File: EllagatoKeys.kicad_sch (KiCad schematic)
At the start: 23 parts, among them J1 Conn_01x10_Socket, SW1 SW_SPST, SW2 SW_SPST, SW3 SW_SPST, SW4 SW_SPST, SW5 RotaryEncoder_Switch_MP, U2 74AHCT1G125

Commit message: Production V1
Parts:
- removed J1: Conn_01x10_Socket, Connector_PinHeader_2.54mm:PinHeader_1x10_P2.54mm_Horizontal, symbol Connector:Conn_01x10_Socket
- added C1: 100n, Capacitor_SMD:C_0805_2012Metric_Pad1.18x1.45mm_HandSolder, symbol Device:C_Small
- added J2: Conn_01x08_Socket, Connector_PinHeader_2.54mm:PinHeader_1x08_P2.54mm_Horizontal, symbol Connector:Conn_01x08_Socket
- added R1: 10k, Resistor_SMD:R_0805_2012Metric_Pad1.20x1.40mm_HandSolder, symbol Device:R_Small
- added TP0: Ground, TestPoint:TestPoint_Keystone_5010-5014_Multipurpose, symbol Connector:TestPoint
- added TP1: LED Data In, TestPoint:TestPoint_Keystone_5010-5014_Multipurpose, symbol Connector:TestPoint_Probe
- added TP2: REnc A, TestPoint:TestPoint_Keystone_5010-5014_Multipurpose, symbol Connector:TestPoint_Probe
- added TP3: REnc B, TestPoint:TestPoint_Keystone_5010-5014_Multipurpose, symbol Connector:TestPoint_Probe
- added TP4: SR PL, TestPoint:TestPoint_Keystone_5010-5014_Multipurpose, symbol Connector:TestPoint_Probe
- added TP5: SR CLK, TestPoint:TestPoint_Keystone_5010-5014_Multipurpose, symbol Connector:TestPoint_Probe
- added TP6: SR DATA, TestPoint:TestPoint_Keystone_5010-5014_Multipurpose, symbol Connector:TestPoint_Probe
- added U1: 74HC165, Package_SO:SOIC-16_3.9x9.9mm_P1.27mm, symbol 74xx:74HC165
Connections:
- net +5V: now also C1.2, J2.8 (Pin_8), U1.16 (VCC)
- net Enc_A: now also J2.5 (Pin_5), TP2.1, U1.4 (D5)
- net Enc_B: now also J2.6 (Pin_6), TP3.1, U1.5 (D6)
- net Enc_Btn: now also U1.3 (D4)
- net GND: now also C1.1, J2.1 (Pin_1), R1.1, TP0.1, U1.15 (~{CE}), U1.8 (GND)
- net Led_Input: now also J2.7 (Pin_7)
- net btn_A: now also U1.12 (D1)
- net btn_B: now also U1.13 (D2)
- net btn_C: now also U1.14 (D3)
- net btn_OnOff: now also U1.11 (D0)
- net at LED5.3 (DIN), U2.4: now also TP1.1
- new net: R1.2, U1.6 (D7)
- new net SR_CK: J2.3 (Pin_3), TP5.1, U1.2 (CP)
- new net SR_D: J2.2 (Pin_2), TP6.1, U1.9 (Q7)
- new net SR_PL: J2.4 (Pin_4), TP4.1, U1.1 (~{PL})
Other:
- moved on the sheet: R10, R11, R8, R9, SW1, SW2, SW3, SW4

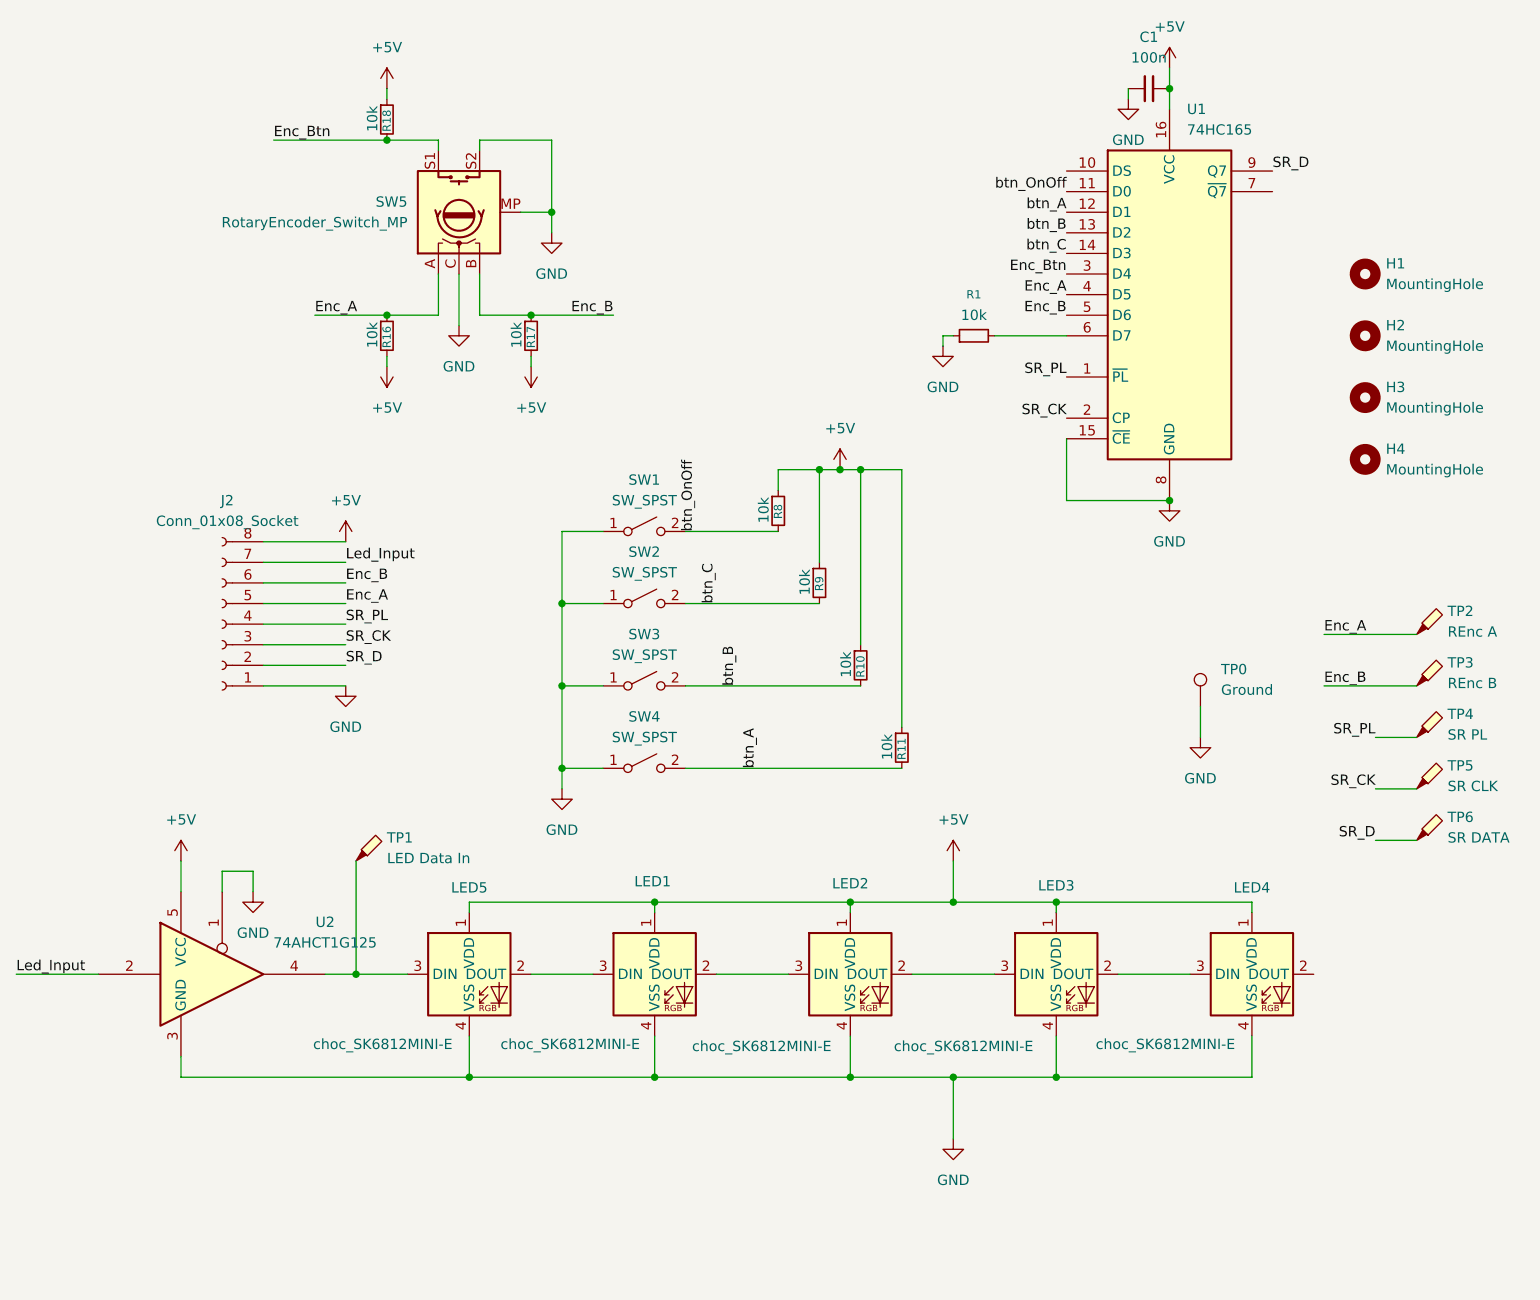
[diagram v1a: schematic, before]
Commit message: +Added Decoupling Cap to LED !!Added connection to VCC for LED2&3 !Restored compoenent labels
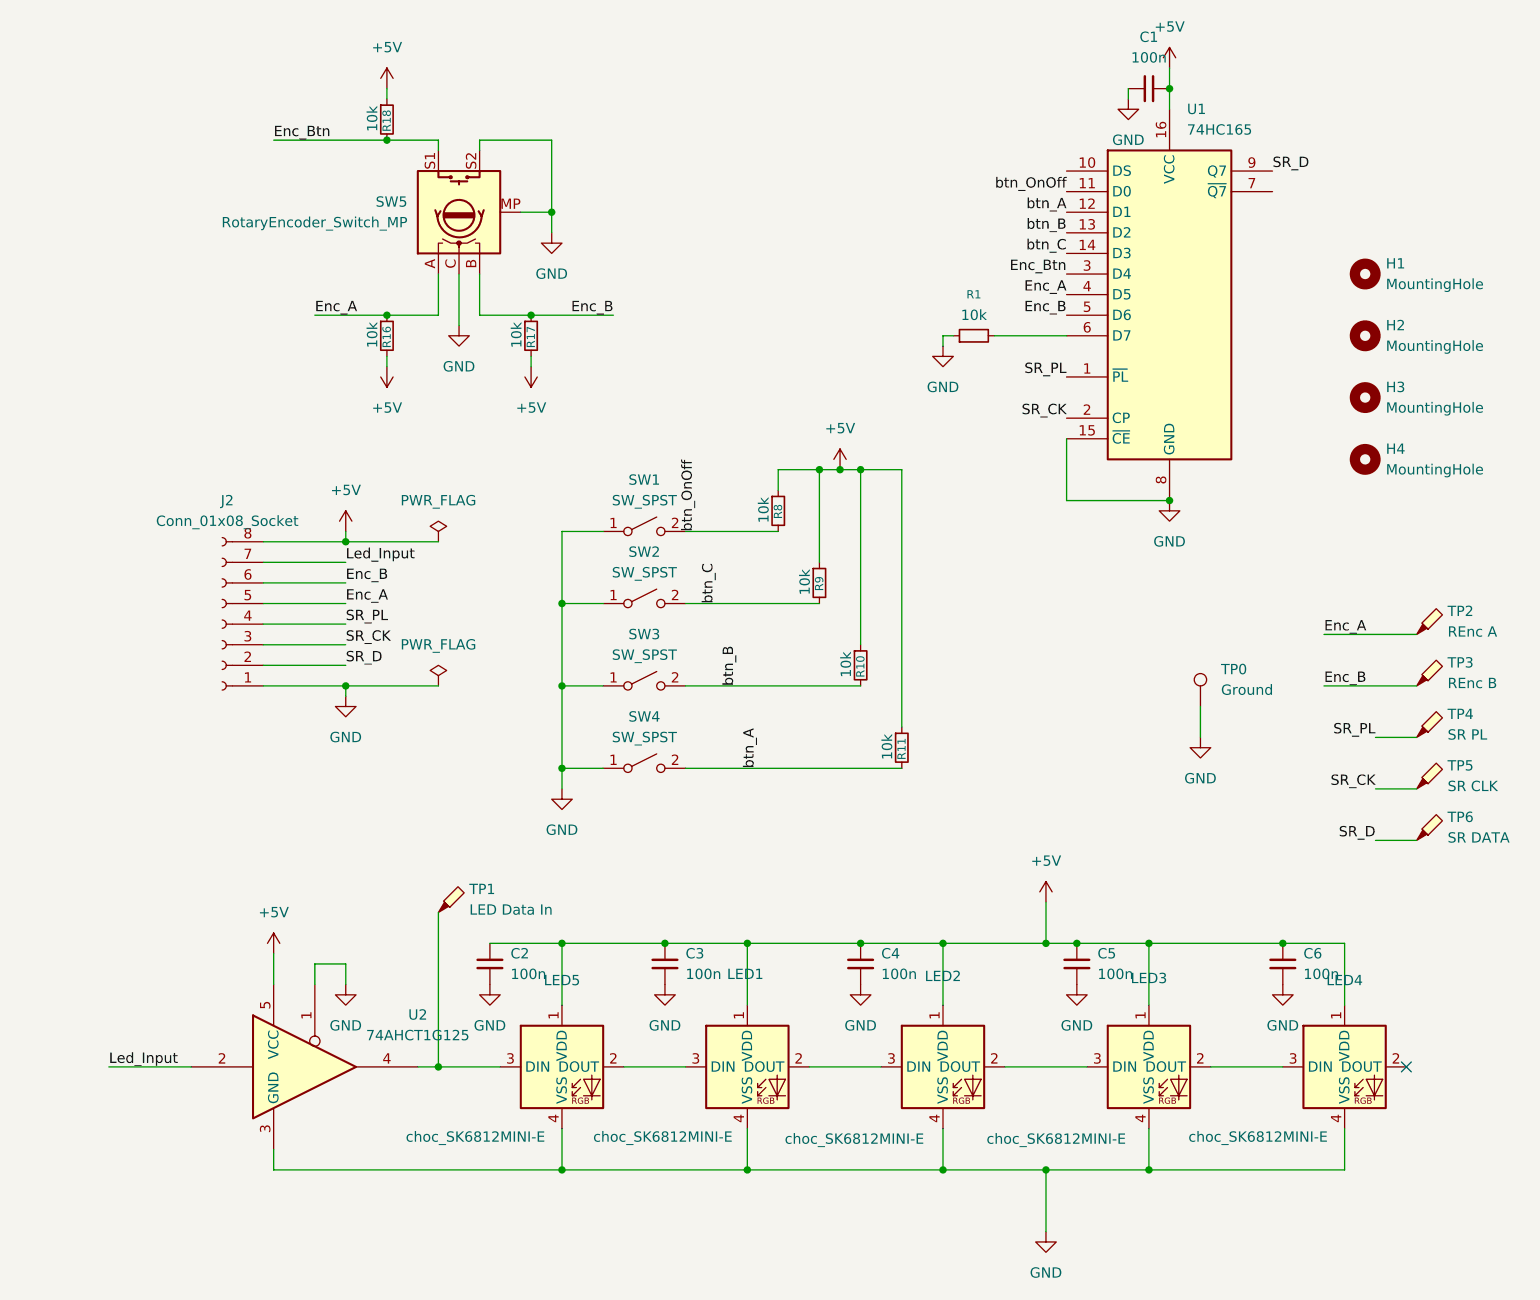
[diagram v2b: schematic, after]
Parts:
- added C2, C3, C4, C5, C6: 100n, Capacitor_SMD:C_0805_2012Metric_Pad1.18x1.45mm_HandSolder, symbol Device:C_Small
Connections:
- net +5V: now also C2.1, C3.1, C4.1, C5.1, C6.1
- net GND: now also C2.2, C3.2, C4.2, C5.2, C6.2
- no-connect marks 0 -> 1
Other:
- moved on the sheet: LED1, LED2, LED3, LED4, LED5, TP1, U2
